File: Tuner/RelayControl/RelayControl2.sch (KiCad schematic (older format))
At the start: 90 parts, among them J3 Conn_01x06, J4 Conn_01x01, J5 Conn_01x01, J6 Conn_01x01, J8 Conn_02x16_Odd_Even, J9 Conn_01x01, U4 MCP23017, U5 ULN2803A, U6 ULN2803A

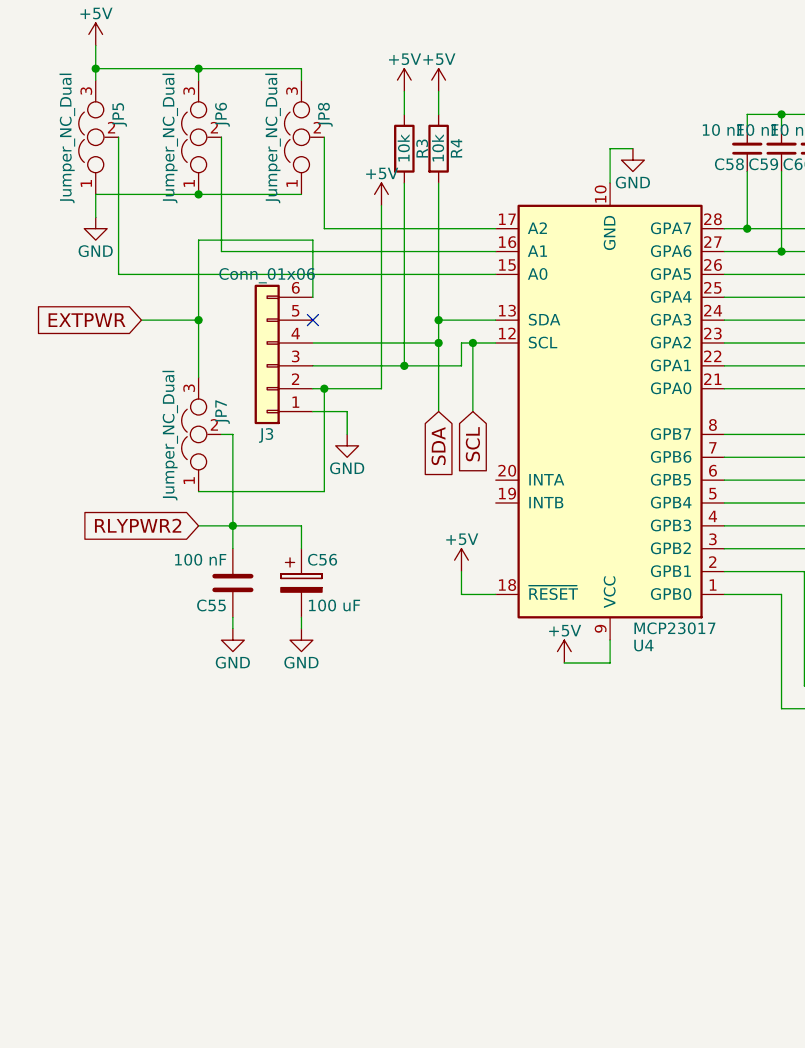
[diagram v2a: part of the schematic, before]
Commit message: JLCPCB order 09232018 - improved grounding - improved I2C cabling - NEO7M port - support for common mode chokes - relay board now has capacitors on all coils
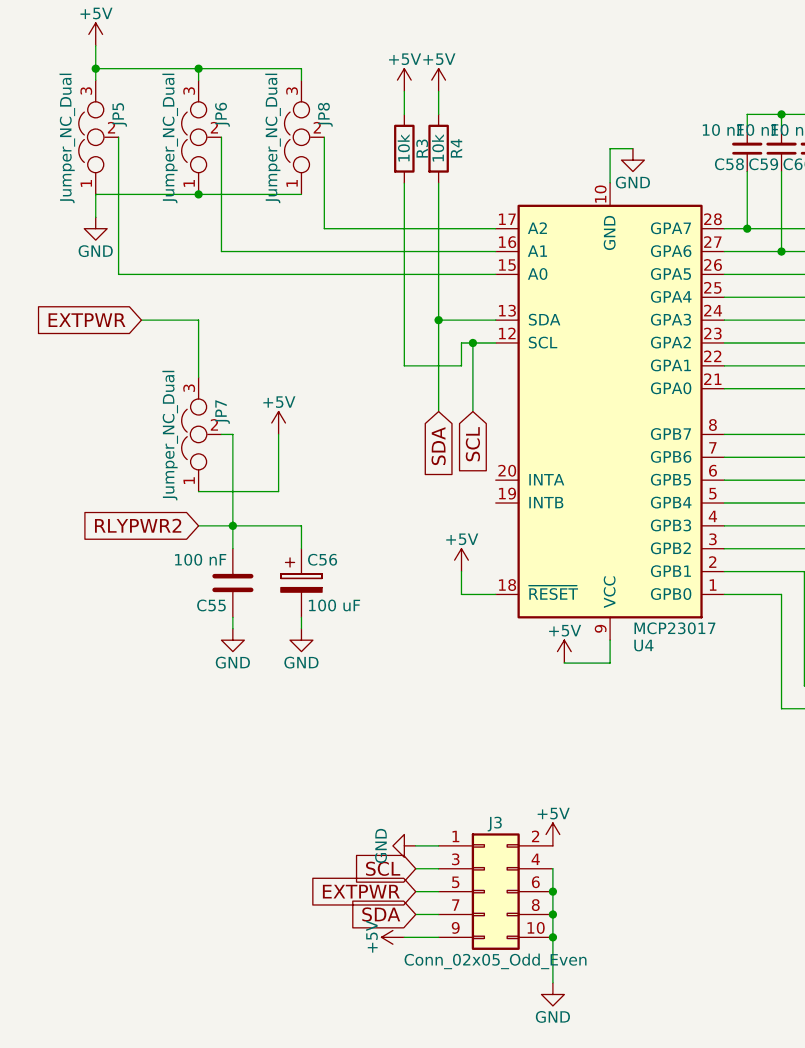
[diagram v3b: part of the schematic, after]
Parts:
- removed J3: Conn_01x06, Connectors_Molex:Molex_KK-6410-06_06x2.54mm_Straight, symbol Conn_01x06
- added J3: Conn_02x05_Odd_Even, Pin_Headers:Pin_Header_Straight_2x05_Pitch2.54mm, symbol Conn_02x05_Odd_Even
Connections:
- net +5V: now also J3.2 (Pin_2), J3.9 (Pin_9)
- net EXTPWR: now also J3.5 (Pin_5)
- net GND: now also J3.1 (Pin_1), J3.10 (Pin_10), J3.4 (Pin_4), J3.6 (Pin_6), J3.8 (Pin_8)
- net SCL: now also J3.3 (Pin_3)
- net SDA: now also J3.7 (Pin_7)
- no-connect marks 1 -> 0
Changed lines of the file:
@@
 $EndComp
 $Comp
-L +5V #PWR21
+L +5V #PWR023
 U 1 1 5B99E946
 P 1050 1050
-F 0 "#PWR21" H 1050 900 50  0001 C CNN
+F 0 "#PWR023" H 1050 900 50  0001 C CNN
 F 1 "+5V" H 1050 1190 50  0000 C CNN
 F 2 "" H 1050 1050 50  0001 C CNN
@@
 $EndComp
 $Comp
-L GND #PWR22
+L GND #PWR024
 U 1 1 5B99E94C
 P 1050 1500
-F 0 "#PWR22" H 1050 1250 50  0001 C CNN
+F 0 "#PWR024" H 1050 1250 50  0001 C CNN
 F 1 "GND" H 1050 1350 50  0000 C CNN
 F 2 "" H 1050 1500 50  0001 C CNN
@@
 $EndComp
 $Comp
-L GND #PWR20
+L GND #PWR025
 U 1 1 5B99E9A6
 P 900 3100
-F 0 "#PWR20" H 900 2850 50  0001 C CNN
+F 0 "#PWR025" H 900 2850 50  0001 C CNN
 F 1 "GND" H 900 2950 50  0000 C CNN
 F 2 "" H 900 3100 50  0001 C CNN
@@
 $EndComp
 $Comp
-L +5V #PWR19
+L +5V #PWR026
 U 1 1 5B99E9AC
 P 900 2350
-F 0 "#PWR19" H 900 2200 50  0001 C CNN
+F 0 "#PWR026" H 900 2200 50  0001 C CNN
 F 1 "+5V" H 900 2490 50  0000 C CNN
 F 2 "" H 900 2350 50  0001 C CNN
@@
 $EndComp
 $Comp
-L GND #PWR25
-U 1 1 5B99E9B2
-P 2000 4050
-F 0 "#PWR25" H 2000 3800 50  0001 C CNN
-F 1 "GND" H 2000 3900 50  0000 C CNN
-F 2 "" H 2000 4050 50  0001 C CNN
-F 3 "" H 2000 4050 50  0001 C CNN
-	1    2000 4050
-	1    0    0    -1
-$EndComp
-$Comp
-L +5V #PWR26
+L +5V #PWR027
 U 1 1 5B99E9B8
-P 2150 3050
-F 0 "#PWR26" H 2150 2900 50  0001 C CNN
-F 1 "+5V" H 2150 3190 50  0000 C CNN
-F 2 "" H 2150 3050 50  0001 C CNN
-F 3 "" H 2150 3050 50  0001 C CNN
-	1    2150 3050
+P 1700 4050
+F 0 "#PWR027" H 1700 3900 50  0001 C CNN
+F 1 "+5V" H 1700 4190 50  0000 C CNN
+F 2 "" H 1700 4050 50  0001 C CNN
+F 3 "" H 1700 4050 50  0001 C CNN
+	1    1700 4050
 	1    0    0    -1
 $EndComp
@@
 $EndComp
 $Comp
-L +5V #PWR28
+L +5V #PWR028
 U 1 1 5B99E9C5
 P 2400 2550
-F 0 "#PWR28" H 2400 2400 50  0001 C CNN
+F 0 "#PWR028" H 2400 2400 50  0001 C CNN
 F 1 "+5V" H 2400 2690 50  0000 C CNN
 F 2 "" H 2400 2550 50  0001 C CNN
@@
 $EndComp
 $Comp
-L +5V #PWR27
+L +5V #PWR029
 U 1 1 5B99E9D2
 P 2250 2550
-F 0 "#PWR27" H 2250 2400 50  0001 C CNN
+F 0 "#PWR029" H 2250 2400 50  0001 C CNN
 F 1 "+5V" H 2250 2690 50  0000 C CNN
 F 2 "" H 2250 2550 50  0001 C CNN
@@
 $EndComp
 $Comp
-L GND #PWR33
+L GND #PWR030
 U 1 1 5B99E9DF
 P 3250 2800
-F 0 "#PWR33" H 3250 2550 50  0001 C CNN
+F 0 "#PWR030" H 3250 2550 50  0001 C CNN
 F 1 "GND" H 3250 2650 50  0000 C CNN
 F 2 "" H 3250 2800 50  0001 C CNN
@@
 	1    3250 2800
 	1    0    0    -1
-$EndComp
-NoConn ~ 1850 3550
-$Comp
-L Conn_01x06 J3
-U 1 1 5B99E9E6
-P 1650 3750
-F 0 "J3" H 1650 4050 50  0000 C CNN
-F 1 "Conn_01x06" H 1650 3350 50  0000 C CNN
-F 2 "Connectors_Molex:Molex_KK-6410-06_06x2.54mm_Straight" H 1650 3750 50  0001 C CNN
-F 3 "" H 1650 3750 50  0001 C CNN
-	1    1650 3750
-	-1   0    0    1
 $EndComp
 $Comp
@@
 RLYPWR2
 $Comp
-L +5V #PWR31
+L +5V #PWR031
 U 1 1 5B99E9F5
 P 2950 5050
-F 0 "#PWR31" H 2950 4900 50  0001 C CNN
+F 0 "#PWR031" H 2950 4900 50  0001 C CNN
 F 1 "+5V" H 2950 5190 50  0000 C CNN
 F 2 "" H 2950 5050 50  0001 C CNN
@@
 $EndComp
 $Comp
-L GND #PWR24
+L GND #PWR032
 U 1 1 5B99E9FB
 P 1800 4900
-F 0 "#PWR24" H 1800 4650 50  0001 C CNN
+F 0 "#PWR032" H 1800 4650 50  0001 C CNN
 F 1 "GND" H 1800 4750 50  0000 C CNN
 F 2 "" H 1800 4900 50  0001 C CNN
@@
 $EndComp
 $Comp
-L GND #PWR23
+L GND #PWR033
 U 1 1 5B99EA0B
 P 1500 4900
-F 0 "#PWR23" H 1500 4650 50  0001 C CNN
+F 0 "#PWR033" H 1500 4650 50  0001 C CNN
 F 1 "GND" H 1500 4750 50  0000 C CNN
 F 2 "" H 1500 4900 50  0001 C CNN
@@
 $EndComp
 $Comp
-L +5V #PWR29
+L +5V #PWR034
 U 1 1 5B99EA11
 P 2500 4650
-F 0 "#PWR29" H 2500 4500 50  0001 C CNN
+F 0 "#PWR034" H 2500 4500 50  0001 C CNN
 F 1 "+5V" H 2500 4790 50  0000 C CNN
 F 2 "" H 2500 4650 50  0001 C CNN
@@
 $EndComp
 $Comp
-L GND #PWR36
+L GND #PWR035
 U 1 1 5B99EA17
 P 8650 5650
-F 0 "#PWR36" H 8650 5400 50  0001 C CNN
+F 0 "#PWR035" H 8650 5400 50  0001 C CNN
 F 1 "GND" H 8650 5500 50  0000 C CNN
 F 2 "" H 8650 5650 50  0001 C CNN
@@
 $EndComp
 $Comp
-L GND #PWR34
+L GND #PWR036
 U 1 1 5B99EB13
 P 5000 2700
-F 0 "#PWR34" H 5000 2450 50  0001 C CNN
+F 0 "#PWR036" H 5000 2450 50  0001 C CNN
 F 1 "GND" H 5000 2550 50  0000 C CNN
 F 2 "" H 5000 2700 50  0001 C CNN
@@
 $EndComp
 $Comp
-L GND #PWR35
+L GND #PWR037
 U 1 1 5B99EBC1
 P 6100 4100
-F 0 "#PWR35" H 6100 3850 50  0001 C CNN
+F 0 "#PWR037" H 6100 3850 50  0001 C CNN
 F 1 "GND" H 6100 3950 50  0000 C CNN
 F 2 "" H 6100 4100 50  0001 C CNN
@@
 	1500 4850 1500 4900
 Connection ~ 1500 4450
-Connection ~ 1350 3550
 Wire Wire Line
 	1100 3550 1350 3550
@@
 Wire Wire Line
 	1450 4050 1500 4050
-Connection ~ 1900 3850
-Wire Wire Line
-	1900 4300 1350 4300
-Wire Wire Line
-	1900 3850 1900 4300
-Wire Wire Line
-	1350 3200 1350 3800
-Wire Wire Line
-	1850 3200 1350 3200
-Wire Wire Line
-	1850 3450 1850 3200
+Wire Wire Line
+	1700 4300 1350 4300
+Wire Wire Line
+	1350 3550 1350 3800
 Connection ~ 2400 3550
 Wire Wire Line
-	2400 3650 1850 3650
-Wire Wire Line
 	2400 3550 2650 3550
-Connection ~ 2250 3750
 Wire Wire Line
 	2250 2950 2250 3750
@@
 	2500 3750 2500 3650
 Wire Wire Line
-	1850 3750 2500 3750
+	2250 3750 2500 3750
 Wire Wire Line
 	3150 2800 3250 2800
 Wire Wire Line
 	3150 2950 3150 2800
-Wire Wire Line
-	2150 3850 2150 3050
-Wire Wire Line
-	1850 3850 2150 3850
-Wire Wire Line
-	2000 3950 2000 4050
-Wire Wire Line
-	1850 3950 2000 3950
 Wire Wire Line
 	1000 3350 2650 3350
@@
 Wire Wire Line
 	2400 2950 2400 3950
-Connection ~ 2400 3650
 $Comp
 L C_Small C108
@@
 Connection ~ 10100 1850
 $Comp
-L GND #PWR30
+L GND #PWR038
 U 1 1 5B97DFC4
 P 2650 1550
-F 0 "#PWR30" H 2650 1300 50  0001 C CNN
+F 0 "#PWR038" H 2650 1300 50  0001 C CNN
 F 1 "GND" H 2650 1400 50  0000 C CNN
 F 2 "" H 2650 1550 50  0001 C CNN
@@
 $EndComp
 $Comp
-L GND #PWR32
+L GND #PWR039
 U 1 1 5B97F132
 P 3000 1550
-F 0 "#PWR32" H 3000 1300 50  0001 C CNN
+F 0 "#PWR039" H 3000 1300 50  0001 C CNN
 F 1 "GND" H 3000 1400 50  0000 C CNN
 F 2 "" H 3000 1550 50  0001 C CNN
@@
 Wire Wire Line
 	3000 1250 3000 1300
+$Comp
+L Conn_02x05_Odd_Even J3
+U 1 1 5BA475AC
+P 2600 6050
+F 0 "J3" H 2650 6350 50  0000 C CNN
+F 1 "Conn_02x05_Odd_Even" H 2650 5750 50  0000 C CNN
+F 2 "Pin_Headers:Pin_Header_Straight_2x05_Pitch2.54mm" H 2600 6050 50  0001 C CNN
+F 3 "" H 2600 6050 50  0001 C CNN
+	1    2600 6050
+	1    0    0    -1
+$EndComp
+$Comp
+L GND #PWR040
+U 1 1 5BA475B3
+P 2300 5850
+F 0 "#PWR040" H 2300 5600 50  0001 C CNN
+F 1 "GND" H 2300 5700 50  0000 C CNN
+F 2 "" H 2300 5850 50  0001 C CNN
+F 3 "" H 2300 5850 50  0001 C CNN
+	1    2300 5850
+	0    1    1    0
+$EndComp
+Wire Wire Line
+	2300 5850 2400 5850
+$Comp
+L GND #PWR041
+U 1 1 5BA475BA
+P 2900 6450
+F 0 "#PWR041" H 2900 6200 50  0001 C CNN
+F 1 "GND" H 2900 6300 50  0000 C CNN
+F 2 "" H 2900 6450 50  0001 C CNN
+F 3 "" H 2900 6450 50  0001 C CNN
+	1    2900 6450
+	1    0    0    -1
+$EndComp
+Wire Wire Line
+	2900 5950 2900 6450
+Connection ~ 2900 6250
+Connection ~ 2900 6150
+Connection ~ 2900 6050
+$Comp
+L +5V #PWR042
+U 1 1 5BA475C4
+P 2900 5850
+F 0 "#PWR042" H 2900 5700 50  0001 C CNN
+F 1 "+5V" H 2900 5990 50  0000 C CNN
+F 2 "" H 2900 5850 50  0001 C CNN
+F 3 "" H 2900 5850 50  0001 C CNN
+	1    2900 5850
+	1    0    0    -1
+$EndComp
+Text GLabel 2300 5950 0    60   Input ~ 0
+SCL
+Wire Wire Line
+	2300 5950 2400 5950
+Text GLabel 2300 6150 0    60   Input ~ 0
+SDA
+Wire Wire Line
+	2300 6150 2400 6150
+Text GLabel 2300 6050 0    60   Input ~ 0
+EXTPWR
+Wire Wire Line
+	2300 6050 2400 6050
+$Comp
+L +5V #PWR043
+U 1 1 5BA475D0
+P 2250 6250
+F 0 "#PWR043" H 2250 6100 50  0001 C CNN
+F 1 "+5V" H 2250 6390 50  0000 C CNN
+F 2 "" H 2250 6250 50  0001 C CNN
+F 3 "" H 2250 6250 50  0001 C CNN
+	1    2250 6250
+	0    -1   -1   0
+$EndComp
+Wire Wire Line
+	2250 6250 2400 6250
+Wire Wire Line
+	1700 4050 1700 4300
 $EndSCHEMATC

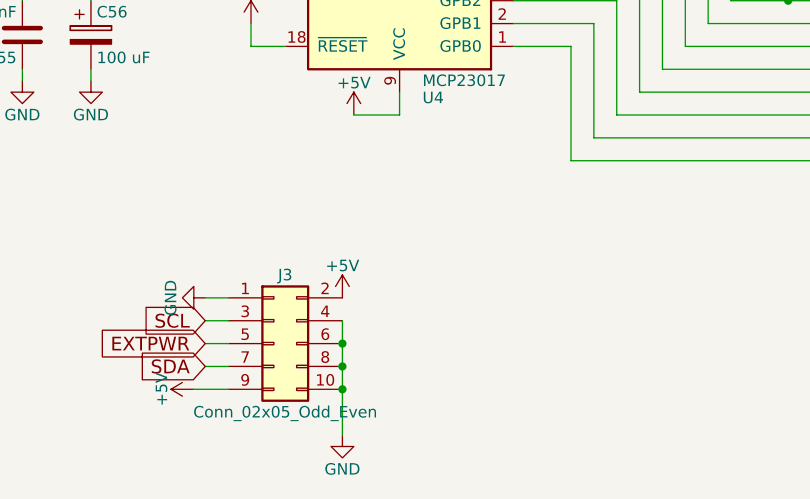
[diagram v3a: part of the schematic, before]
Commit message: Changed I2C cable pinoutgit add Tunergit add Tuner Also added ICOM rig support
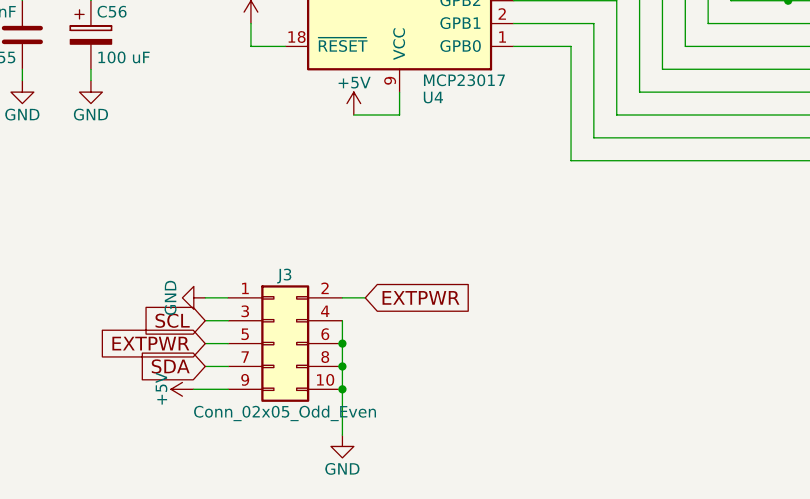
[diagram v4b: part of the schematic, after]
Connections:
- net +5V: no longer J3.2 (Pin_2)
- net EXTPWR: now also J3.2 (Pin_2)
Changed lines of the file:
@@
 $EndComp
 $Comp
-L +5V #PWR023
+L +5V #PWR022
 U 1 1 5B99E946
 P 1050 1050
-F 0 "#PWR023" H 1050 900 50  0001 C CNN
+F 0 "#PWR022" H 1050 900 50  0001 C CNN
 F 1 "+5V" H 1050 1190 50  0000 C CNN
 F 2 "" H 1050 1050 50  0001 C CNN
@@
 $EndComp
 $Comp
-L GND #PWR024
+L GND #PWR023
 U 1 1 5B99E94C
 P 1050 1500
-F 0 "#PWR024" H 1050 1250 50  0001 C CNN
+F 0 "#PWR023" H 1050 1250 50  0001 C CNN
 F 1 "GND" H 1050 1350 50  0000 C CNN
 F 2 "" H 1050 1500 50  0001 C CNN
@@
 $EndComp
 $Comp
-L GND #PWR025
+L GND #PWR024
 U 1 1 5B99E9A6
 P 900 3100
-F 0 "#PWR025" H 900 2850 50  0001 C CNN
+F 0 "#PWR024" H 900 2850 50  0001 C CNN
 F 1 "GND" H 900 2950 50  0000 C CNN
 F 2 "" H 900 3100 50  0001 C CNN
@@
 $EndComp
 $Comp
-L +5V #PWR026
+L +5V #PWR025
 U 1 1 5B99E9AC
 P 900 2350
-F 0 "#PWR026" H 900 2200 50  0001 C CNN
+F 0 "#PWR025" H 900 2200 50  0001 C CNN
 F 1 "+5V" H 900 2490 50  0000 C CNN
 F 2 "" H 900 2350 50  0001 C CNN
@@
 $EndComp
 $Comp
-L +5V #PWR027
+L +5V #PWR026
 U 1 1 5B99E9B8
 P 1700 4050
-F 0 "#PWR027" H 1700 3900 50  0001 C CNN
+F 0 "#PWR026" H 1700 3900 50  0001 C CNN
 F 1 "+5V" H 1700 4190 50  0000 C CNN
 F 2 "" H 1700 4050 50  0001 C CNN
@@
 $EndComp
 $Comp
-L +5V #PWR028
+L +5V #PWR027
 U 1 1 5B99E9C5
 P 2400 2550
-F 0 "#PWR028" H 2400 2400 50  0001 C CNN
+F 0 "#PWR027" H 2400 2400 50  0001 C CNN
 F 1 "+5V" H 2400 2690 50  0000 C CNN
 F 2 "" H 2400 2550 50  0001 C CNN
@@
 $EndComp
 $Comp
-L +5V #PWR029
+L +5V #PWR028
 U 1 1 5B99E9D2
 P 2250 2550
-F 0 "#PWR029" H 2250 2400 50  0001 C CNN
+F 0 "#PWR028" H 2250 2400 50  0001 C CNN
 F 1 "+5V" H 2250 2690 50  0000 C CNN
 F 2 "" H 2250 2550 50  0001 C CNN
@@
 $EndComp
 $Comp
-L GND #PWR030
+L GND #PWR029
 U 1 1 5B99E9DF
 P 3250 2800
-F 0 "#PWR030" H 3250 2550 50  0001 C CNN
+F 0 "#PWR029" H 3250 2550 50  0001 C CNN
 F 1 "GND" H 3250 2650 50  0000 C CNN
 F 2 "" H 3250 2800 50  0001 C CNN
@@
 RLYPWR2
 $Comp
-L +5V #PWR031
+L +5V #PWR030
 U 1 1 5B99E9F5
 P 2950 5050
-F 0 "#PWR031" H 2950 4900 50  0001 C CNN
+F 0 "#PWR030" H 2950 4900 50  0001 C CNN
 F 1 "+5V" H 2950 5190 50  0000 C CNN
 F 2 "" H 2950 5050 50  0001 C CNN
@@
 $EndComp
 $Comp
-L GND #PWR032
+L GND #PWR031
 U 1 1 5B99E9FB
 P 1800 4900
-F 0 "#PWR032" H 1800 4650 50  0001 C CNN
+F 0 "#PWR031" H 1800 4650 50  0001 C CNN
 F 1 "GND" H 1800 4750 50  0000 C CNN
 F 2 "" H 1800 4900 50  0001 C CNN
@@
 $EndComp
 $Comp
-L GND #PWR033
+L GND #PWR032
 U 1 1 5B99EA0B
 P 1500 4900
-F 0 "#PWR033" H 1500 4650 50  0001 C CNN
+F 0 "#PWR032" H 1500 4650 50  0001 C CNN
 F 1 "GND" H 1500 4750 50  0000 C CNN
 F 2 "" H 1500 4900 50  0001 C CNN
@@
 $EndComp
 $Comp
-L +5V #PWR034
+L +5V #PWR033
 U 1 1 5B99EA11
 P 2500 4650
-F 0 "#PWR034" H 2500 4500 50  0001 C CNN
+F 0 "#PWR033" H 2500 4500 50  0001 C CNN
 F 1 "+5V" H 2500 4790 50  0000 C CNN
 F 2 "" H 2500 4650 50  0001 C CNN
@@
 $EndComp
 $Comp
-L GND #PWR035
+L GND #PWR034
 U 1 1 5B99EA17
 P 8650 5650
-F 0 "#PWR035" H 8650 5400 50  0001 C CNN
+F 0 "#PWR034" H 8650 5400 50  0001 C CNN
 F 1 "GND" H 8650 5500 50  0000 C CNN
 F 2 "" H 8650 5650 50  0001 C CNN
@@
 $EndComp
 $Comp
-L GND #PWR036
+L GND #PWR035
 U 1 1 5B99EB13
 P 5000 2700
-F 0 "#PWR036" H 5000 2450 50  0001 C CNN
+F 0 "#PWR035" H 5000 2450 50  0001 C CNN
 F 1 "GND" H 5000 2550 50  0000 C CNN
 F 2 "" H 5000 2700 50  0001 C CNN
@@
 $EndComp
 $Comp
-L GND #PWR037
+L GND #PWR036
 U 1 1 5B99EBC1
 P 6100 4100
-F 0 "#PWR037" H 6100 3850 50  0001 C CNN
+F 0 "#PWR036" H 6100 3850 50  0001 C CNN
 F 1 "GND" H 6100 3950 50  0000 C CNN
 F 2 "" H 6100 4100 50  0001 C CNN
@@
 Connection ~ 10100 1850
 $Comp
-L GND #PWR038
+L GND #PWR037
 U 1 1 5B97DFC4
 P 2650 1550
-F 0 "#PWR038" H 2650 1300 50  0001 C CNN
+F 0 "#PWR037" H 2650 1300 50  0001 C CNN
 F 1 "GND" H 2650 1400 50  0000 C CNN
 F 2 "" H 2650 1550 50  0001 C CNN
@@
 $EndComp
 $Comp
-L GND #PWR039
+L GND #PWR038
 U 1 1 5B97F132
 P 3000 1550
-F 0 "#PWR039" H 3000 1300 50  0001 C CNN
+F 0 "#PWR038" H 3000 1300 50  0001 C CNN
 F 1 "GND" H 3000 1400 50  0000 C CNN
 F 2 "" H 3000 1550 50  0001 C CNN
@@
 $EndComp
 $Comp
-L GND #PWR040
+L GND #PWR039
 U 1 1 5BA475B3
 P 2300 5850
-F 0 "#PWR040" H 2300 5600 50  0001 C CNN
+F 0 "#PWR039" H 2300 5600 50  0001 C CNN
 F 1 "GND" H 2300 5700 50  0000 C CNN
 F 2 "" H 2300 5850 50  0001 C CNN
@@
 	2300 5850 2400 5850
 $Comp
-L GND #PWR041
+L GND #PWR040
 U 1 1 5BA475BA
 P 2900 6450
-F 0 "#PWR041" H 2900 6200 50  0001 C CNN
+F 0 "#PWR040" H 2900 6200 50  0001 C CNN
 F 1 "GND" H 2900 6300 50  0000 C CNN
 F 2 "" H 2900 6450 50  0001 C CNN
@@
 Connection ~ 2900 6150
 Connection ~ 2900 6050
-$Comp
-L +5V #PWR042
-U 1 1 5BA475C4
-P 2900 5850
-F 0 "#PWR042" H 2900 5700 50  0001 C CNN
-F 1 "+5V" H 2900 5990 50  0000 C CNN
-F 2 "" H 2900 5850 50  0001 C CNN
-F 3 "" H 2900 5850 50  0001 C CNN
-	1    2900 5850
-	1    0    0    -1
-$EndComp
 Text GLabel 2300 5950 0    60   Input ~ 0
 SCL
@@
 	2300 6050 2400 6050
 $Comp
-L +5V #PWR043
+L +5V #PWR042
 U 1 1 5BA475D0
 P 2250 6250
-F 0 "#PWR043" H 2250 6100 50  0001 C CNN
+F 0 "#PWR042" H 2250 6100 50  0001 C CNN
 F 1 "+5V" H 2250 6390 50  0000 C CNN
 F 2 "" H 2250 6250 50  0001 C CNN
@@
 Wire Wire Line
 	1700 4050 1700 4300
+Text GLabel 3000 5850 2    60   Input ~ 0
+EXTPWR
+Wire Wire Line
+	3000 5850 2900 5850
 $EndSCHEMATC
